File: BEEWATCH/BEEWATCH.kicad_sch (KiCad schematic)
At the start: 0 parts

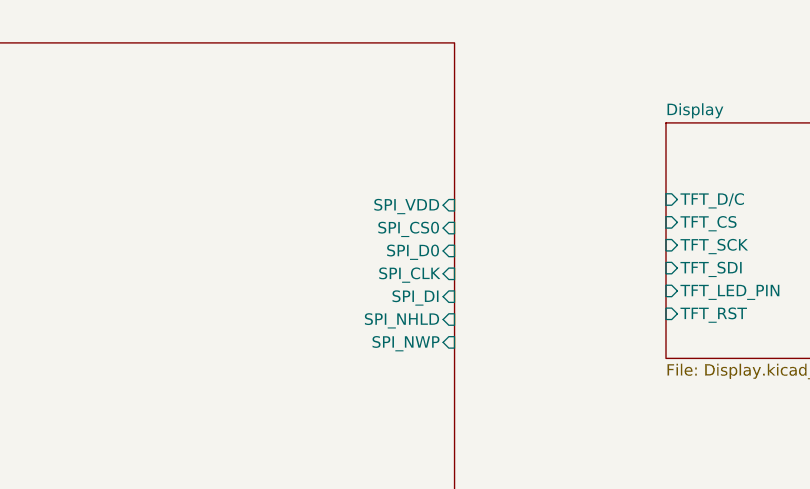
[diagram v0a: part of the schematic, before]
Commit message: GPS Removed
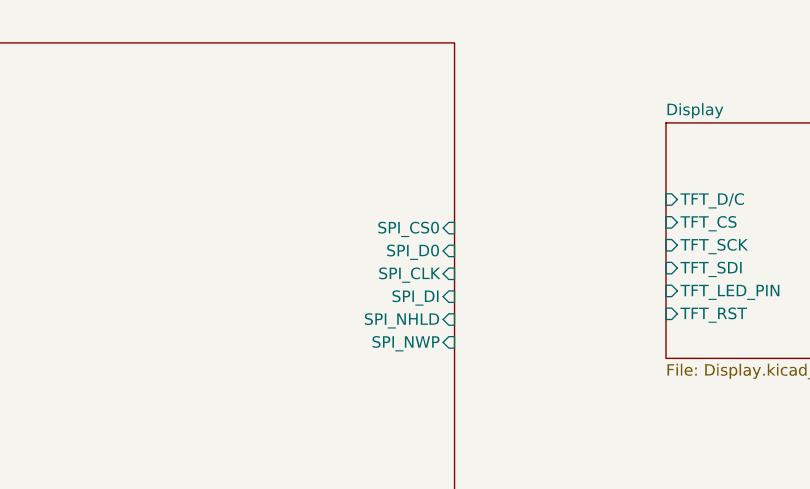
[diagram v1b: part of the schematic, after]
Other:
- sheet ESP32 ports: added none; removed SPI_VDD
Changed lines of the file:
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@@
       (effects (font (size 1.27 1.27)) (justify left top))
-    )
-    (pin "SPI_VDD" input (at 183.515 45.72 0)
-      (effects (font (size 1.27 1.27)) (justify right))
     )
     (pin "SPI_CS0" input (at 183.515 48.26 0)
